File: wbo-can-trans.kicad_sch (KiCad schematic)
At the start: 7 parts, among them U15 TJA1051T-3

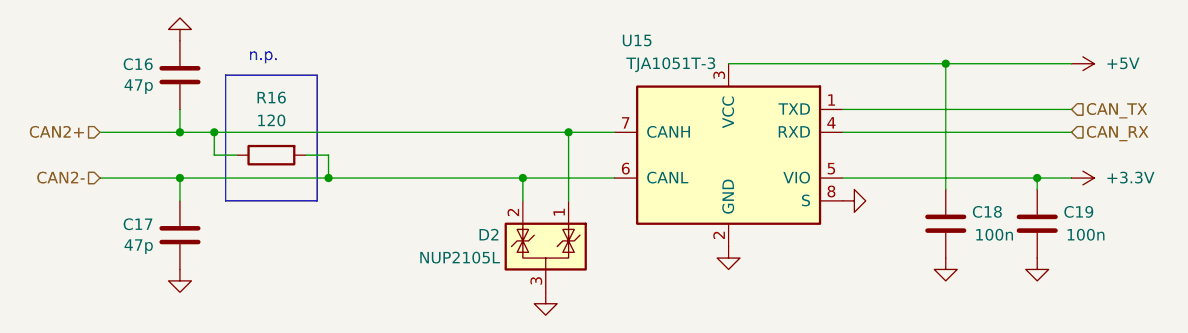
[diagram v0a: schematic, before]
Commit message: Changes to discrete VR
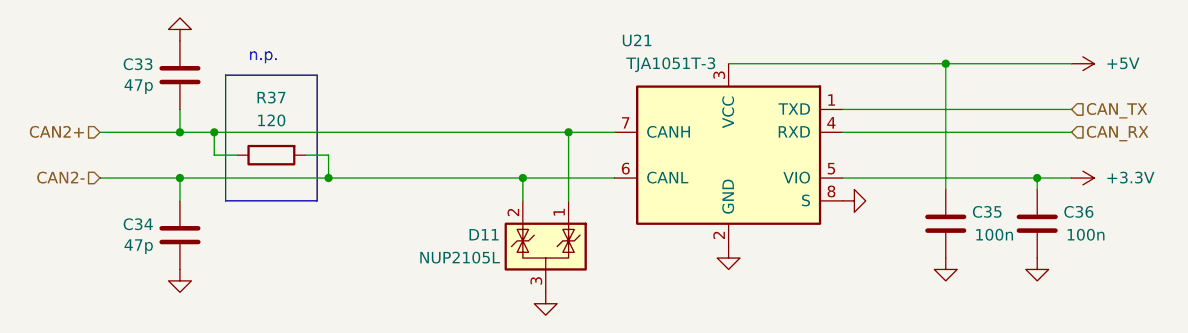
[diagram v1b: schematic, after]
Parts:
- renumbered C16 to C33, C17 to C34, C18 to C35, C19 to C36, D2 to D11, R16 to R37, U15 to U21

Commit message: fixed issues: 10, 6, 5, 4 and 2
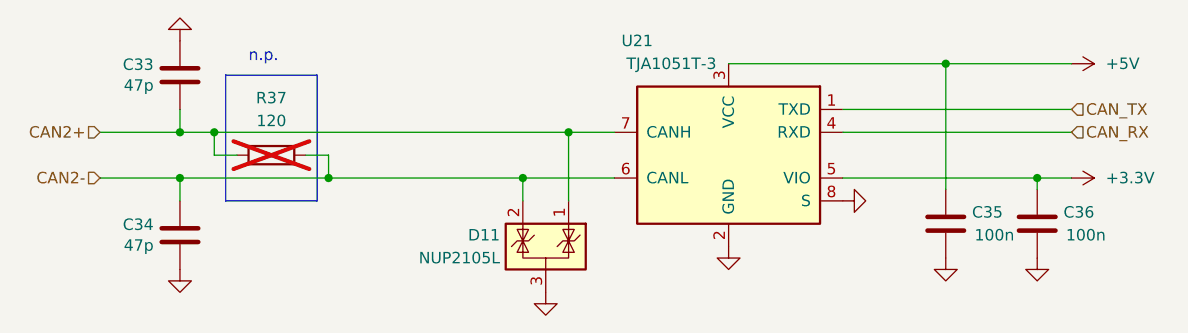
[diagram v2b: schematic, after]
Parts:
- R37: now not fitted

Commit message: Fixed trigger scope
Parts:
- renumbered C33 to C29, C34 to C30, C35 to C31, C36 to C32, D11 to D10, R37 to R36, U21 to U20
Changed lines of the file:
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@@
 (kicad_sch
-	(version 20231120)
+	(version 20250114)
 	(generator "eeschema")
-	(generator_version "8.0")
+	(generator_version "9.0")
 	(paper "A4")
 	(title_block
@@
 		(company "FutureProofPerformance.com")
 	)
+	(text "n.p."
+		(exclude_from_sim no)
+		(at 113.03 76.2 0)
+		(effects
+			(font
+				(size 1.27 1.27)
+			)
+			(justify left bottom)
+		)
+	)
 	(junction
 		(at 148.59 83.82)
@@
 		)
 	)
-	(text "n.p."
-		(exclude_from_sim no)
-		(at 113.03 76.2 0)
+	(hierarchical_label "CAN_RX"
+		(shape input)
+		(at 204.47 83.82 0)
 		(effects
 			(font
 				(size 1.27 1.27)
 			)
-			(justify left bottom)
-		)
-	)
-	(hierarchical_label "CAN_RX"
+			(justify left)
+		)
+	)
+	(hierarchical_label "CAN2-"
 		(shape input)
-		(at 204.47 83.82 0)
-		(fields_autoplaced yes)
+		(at 96.52 88.9 180)
 		(effects
 			(font
 				(size 1.27 1.27)
 			)
-			(justify left)
-		)
-	)
-	(hierarchical_label "CAN2-"
+			(justify right)
+		)
+	)
+	(hierarchical_label "CAN2+"
 		(shape input)
-		(at 96.52 88.9 180)
-		(fields_autoplaced yes)
+		(at 96.52 83.82 180)
 		(effects
 			(font
@@
 		)
 	)
-	(hierarchical_label "CAN2+"
+	(hierarchical_label "CAN_TX"
 		(shape input)
-		(at 96.52 83.82 180)
-		(fields_autoplaced yes)
+		(at 204.47 81.28 0)
 		(effects
 			(font
 				(size 1.27 1.27)
 			)
-			(justify right)
-		)
-	)
-	(hierarchical_label "CAN_TX"
-		(shape input)
-		(at 204.47 81.28 0)
-		(fields_autoplaced yes)
-		(effects
-			(font
-				(size 1.27 1.27)
-			)
 			(justify left)
 		)
@@
 		(dnp no)
 		(fields_autoplaced yes)
-		(property "Reference" "#PWR0149"
+		(property "Reference" "#PWR0140"
 			(at 105.41 67.31 0)
 			(effects
@@
 		(dnp no)
 		(fields_autoplaced yes)
-		(property "Reference" "#PWR0153"
+		(property "Reference" "#PWR0144"
 			(at 185.42 91.44 0)
 			(effects
@@
 		(dnp no)
 		(fields_autoplaced yes)
-		(property "Reference" "#PWR0155"
+		(property "Reference" "#PWR0146"
 			(at 200.66 104.14 0)
 			(effects
@@
 		(on_board yes)
 		(dnp no)
-		(property "Reference" "D11"
+		(property "Reference" "D10"
 			(at 140.97 95.25 0)
 			(effects
@@
 		(dnp no)
 		(fields_autoplaced yes)
-		(property "Reference" "#PWR0151"
+		(property "Reference" "#PWR0142"
 			(at 146.05 107.95 0)
 			(effects
@@
 		(dnp no)
 		(fields_autoplaced yes)
-		(property "Reference" "#PWR0154"
+		(property "Reference" "#PWR0145"
 			(at 190.5 104.14 0)
 			(effects
@@
 		(on_board yes)
 		(dnp no)
-		(property "Reference" "C33"
+		(property "Reference" "C29"
 			(at 102.489 76.3016 0)
 			(effects
@@
 		(on_board yes)
 		(dnp no)
-		(property "Reference" "C34"
+		(property "Reference" "C30"
 			(at 102.489 94.0816 0)
 			(effects
@@
 		(on_board yes)
 		(dnp no)
-		(property "Reference" "C35"
+		(property "Reference" "C31"
 			(at 196.85 92.71 0)
 			(effects
@@
 		(dnp no)
 		(fields_autoplaced yes)
-		(property "Reference" "#PWR0157"
+		(property "Reference" "#PWR0148"
 			(at 200.66 88.9 0)
 			(effects
@@
 		(dnp no)
 		(fields_autoplaced yes)
-		(property "Reference" "#PWR0150"
+		(property "Reference" "#PWR0141"
 			(at 105.41 105.41 0)
 			(effects
@@
 		(dnp no)
 		(fields_autoplaced yes)
-		(property "Reference" "#PWR0156"
+		(property "Reference" "#PWR0147"
 			(at 200.66 76.2 0)
 			(effects
@@
 		(on_board yes)
 		(dnp no)
-		(property "Reference" "C36"
+		(property "Reference" "C32"
 			(at 207.01 92.71 0)
 			(effects
@@
 		(on_board yes)
 		(dnp no)
-		(property "Reference" "U21"
+		(property "Reference" "U20"
 			(at 156.21 73.66 0)
 			(effects
@@
 		(dnp no)
 		(fields_autoplaced yes)
-		(property "Reference" "#PWR0152"
+		(property "Reference" "#PWR0143"
 			(at 166.37 102.87 0)
 			(effects
@@
 		(on_board yes)
 		(dnp yes)
-		(property "Reference" "R37"
+		(property "Reference" "R36"
 			(at 115.57 80.01 90)
 			(effects
